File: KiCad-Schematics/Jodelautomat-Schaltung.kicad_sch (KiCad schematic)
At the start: 70 parts, among them J1 AudioJack3, J2 I2C_5V_01x04, J3 Barrel_Jack, J4 Screw_Terminal_01x02, J5 USART_Full_01x06, Q1 BC337, Q2 BC337, Q3 BC337, Q4 BC337, Q5 BC337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

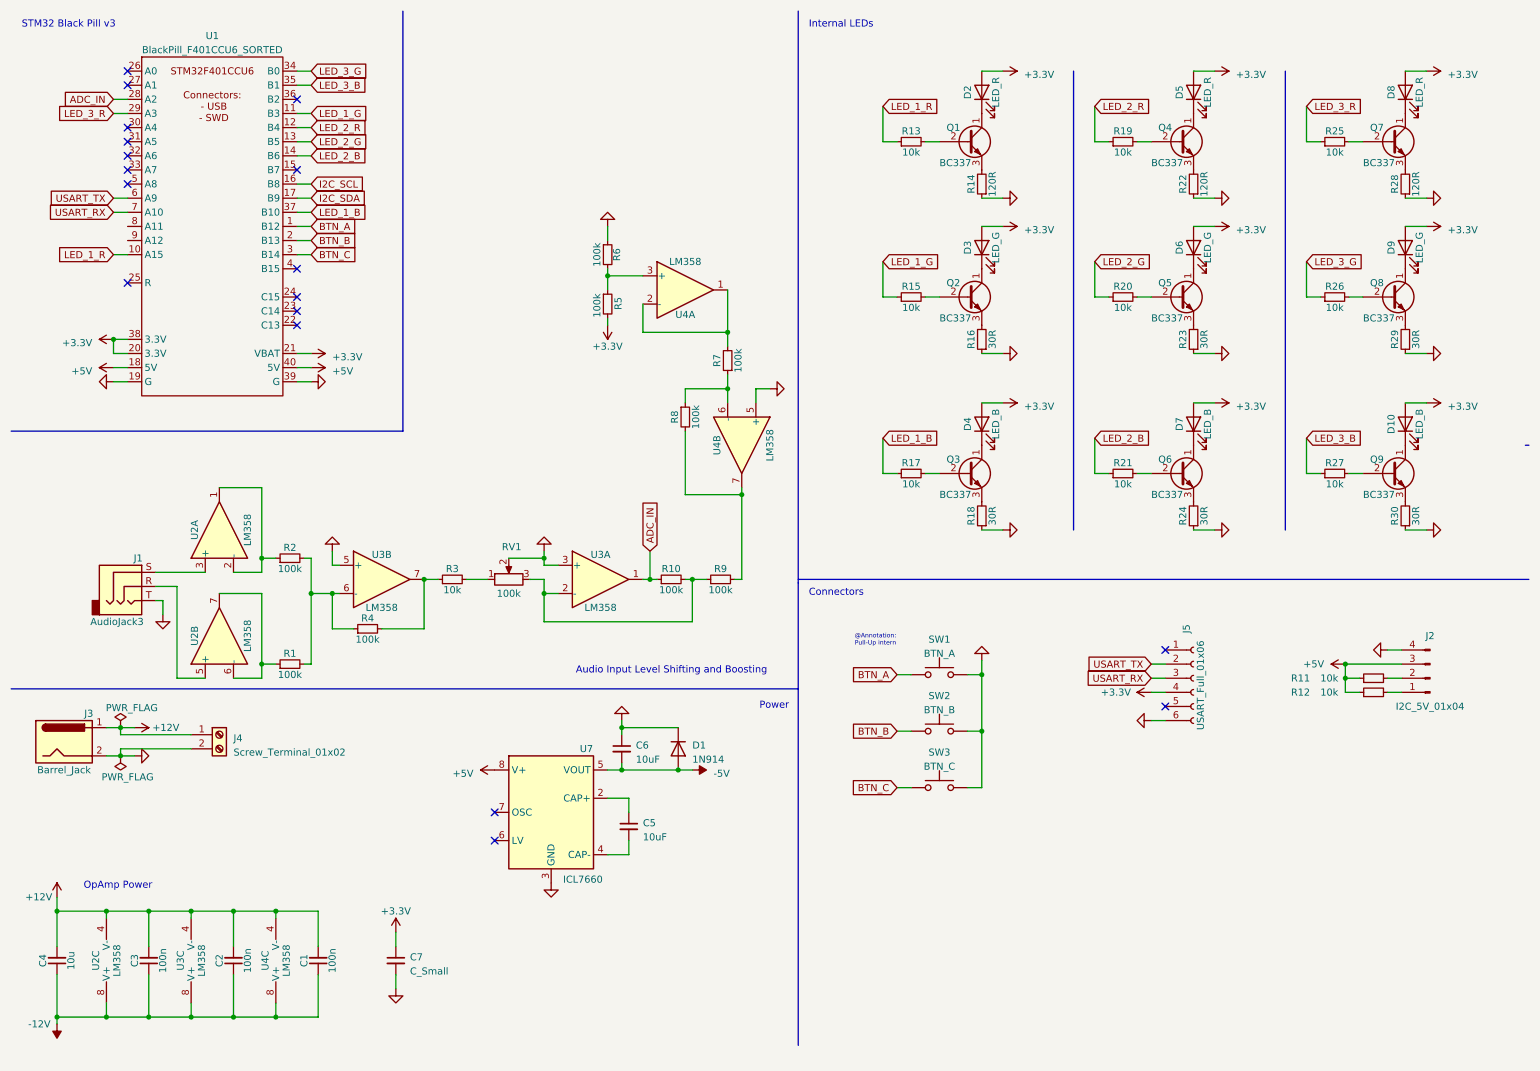
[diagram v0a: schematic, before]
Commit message: added uart fft output
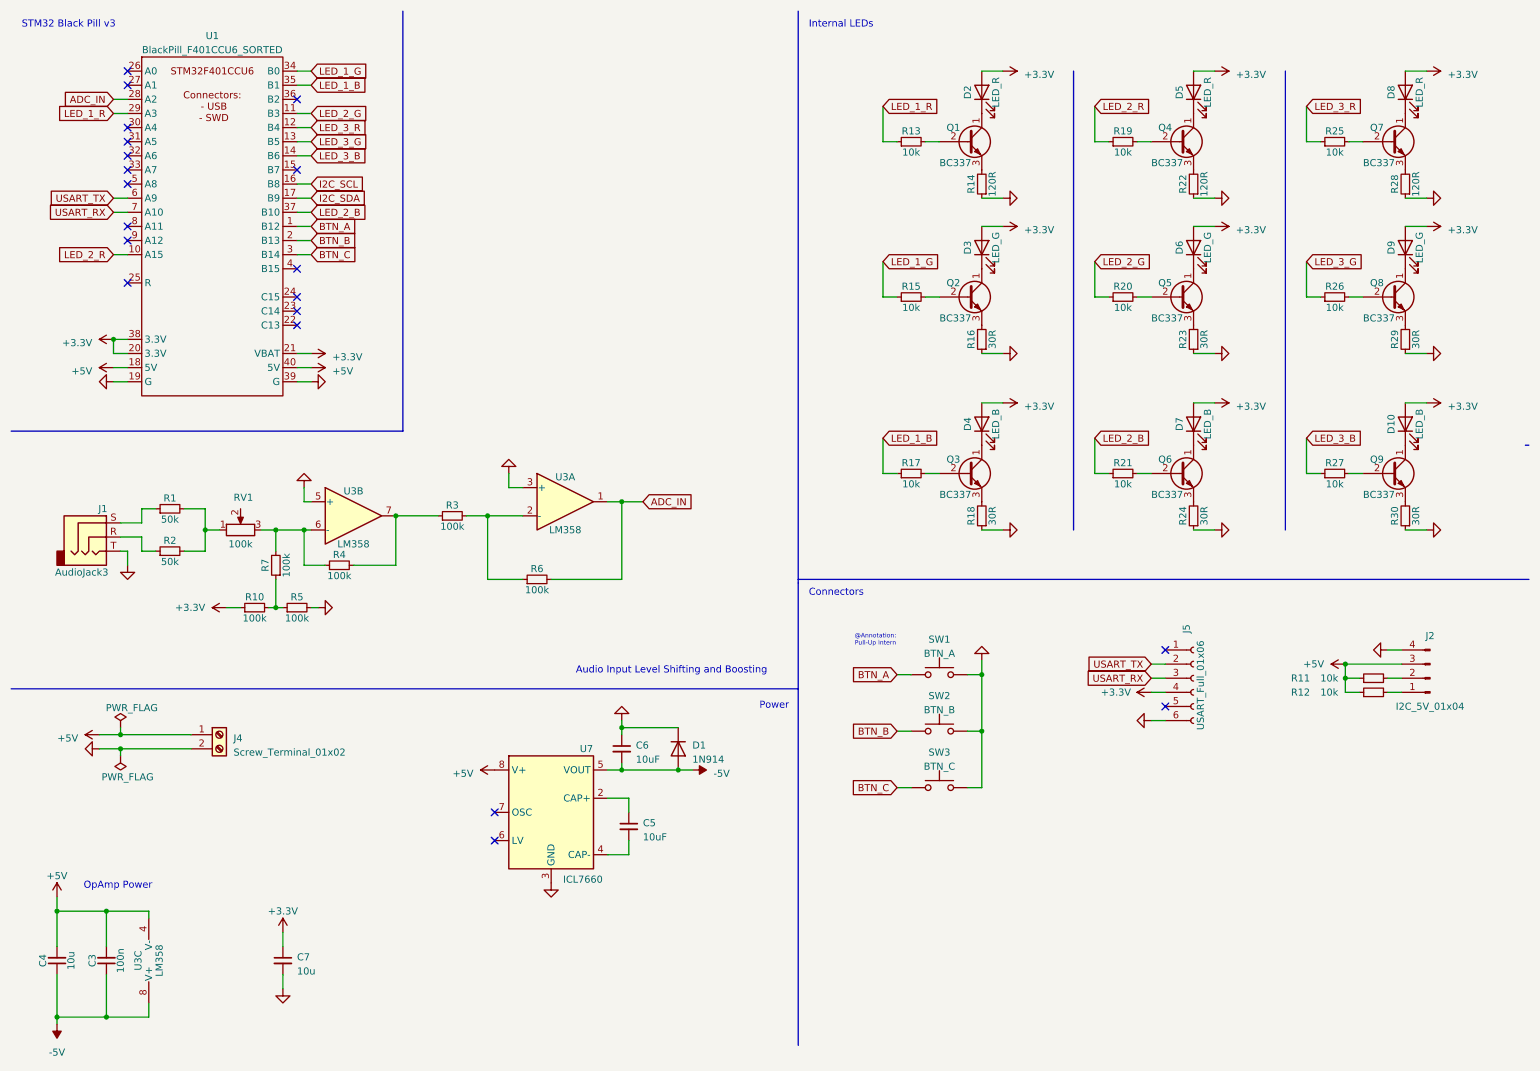
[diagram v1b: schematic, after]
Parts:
- removed C1, C2: 100n, Capacitor_SMD:C_0603_1608Metric, symbol Device:C_Small
- removed J3: Barrel_Jack, Connector_BarrelJack:BarrelJack_SwitchcraftConxall_RAPC10U_Horizontal, symbol Connector:Barrel_Jack
- removed R8, R9: 100k, Resistor_SMD:R_0402_1005Metric, symbol Device:R_Small
- removed U2, U4: LM358, Package_SO:SOIC-8_3.9x4.9mm_P1.27mm, symbol Amplifier_Operational:LM358
- C7: value C_Small -> 10u; footprint (none) -> Capacitor_SMD:C_0603_1608Metric
- D10, D2, D3, D4, D5, D6, D7, D8, D9: footprint (none) -> LED_SMD:LED_2010_5025Metric
- J2: footprint (none) -> Connector_Molex:Molex_PicoBlade_53047-0410_1x04_P1.25mm_Vertical
- J5: footprint (none) -> Connector_Molex:Molex_PicoBlade_53047-0610_1x06_P1.25mm_Vertical
- R1, R2: value 100k -> 50k
- R11, R12, R13, R15, R17, R19, R20, R21, R25, R26, R27: footprint (none) -> Resistor_SMD:R_0402_1005Metric
- R14, R16, R18, R22, R23, R24, R28, R29, R30: footprint (none) -> Resistor_SMD:R_0603_1608Metric
- R3: value 10k -> 100k
- SW1, SW2, SW3: footprint (none) -> Button_Switch_THT:SW_PUSH_6mm
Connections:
- net +12V is gone; now on net +5V: C3.2, C4.2, J4.1 (Pin_1), U3.4 (V-)
- net -12V is gone; now on net -5V: C3.1, C4.1, U3.8 (V+)
- net +3.3V: now also R10.1; no longer R5.2
- net ADC_IN: now also R6.2; no longer R10.1
- net GND: now also R5.2; no longer R6.1, RV1.2
- net LED_1_B: now also U1.35 (B1); no longer U1.37 (B10)
- net LED_1_G: now also U1.34 (B0); no longer U1.11 (B3)
- net LED_1_R: now also U1.29 (A3); no longer U1.10 (A15)
- net LED_2_B: now also U1.37 (B10); no longer U1.14 (B6)
- net LED_2_G: now also U1.11 (B3); no longer U1.13 (B5)
- net LED_2_R: now also U1.10 (A15); no longer U1.12 (B4)
- net LED_3_B: now also U1.14 (B6); no longer U1.35 (B1)
- net LED_3_G: now also U1.13 (B5); no longer U1.34 (B0)
- net LED_3_R: now also U1.12 (B4); no longer U1.29 (A3)
- net at R7.1: now also R10.2, R5.1
- net at R4.1, U3.6 (-): now also R7.2, RV1.3; no longer R1.2, R2.2
- net at RV1.1: now also R1.2, R2.2; no longer R3.2
- net at J1.R: now also R2.1
- net at R1.1: now also J1.S
- new net: R3.2, R6.1, U3.2 (-)
- no-connect marks 18 -> 20
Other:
- moved on the sheet: C3, C7, J1, R1, R10, R2, R4, RV1, U3A, U3B, U3C

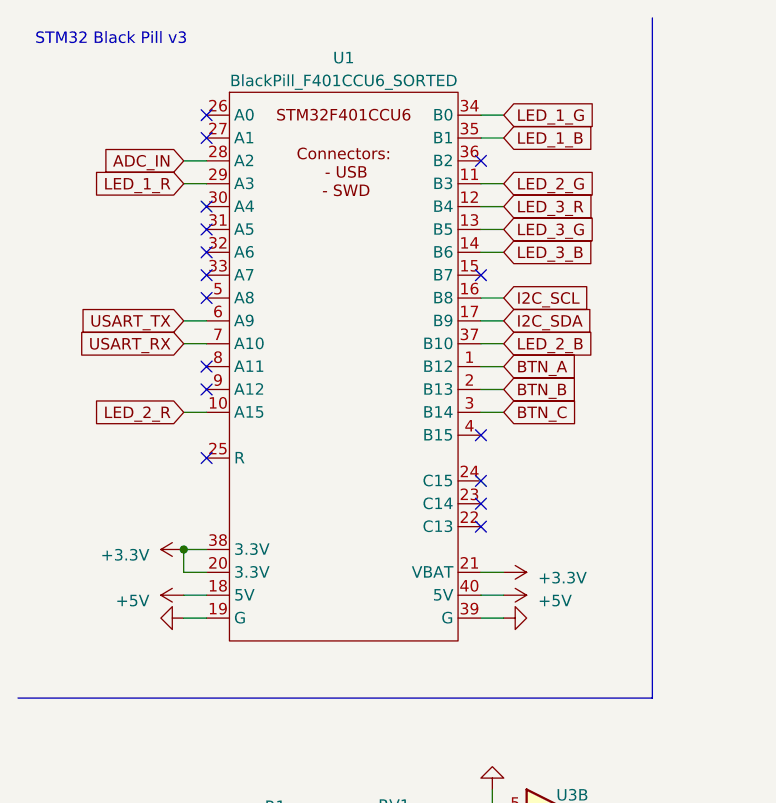
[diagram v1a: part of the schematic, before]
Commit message: moving pins around to have a better breadboard layout
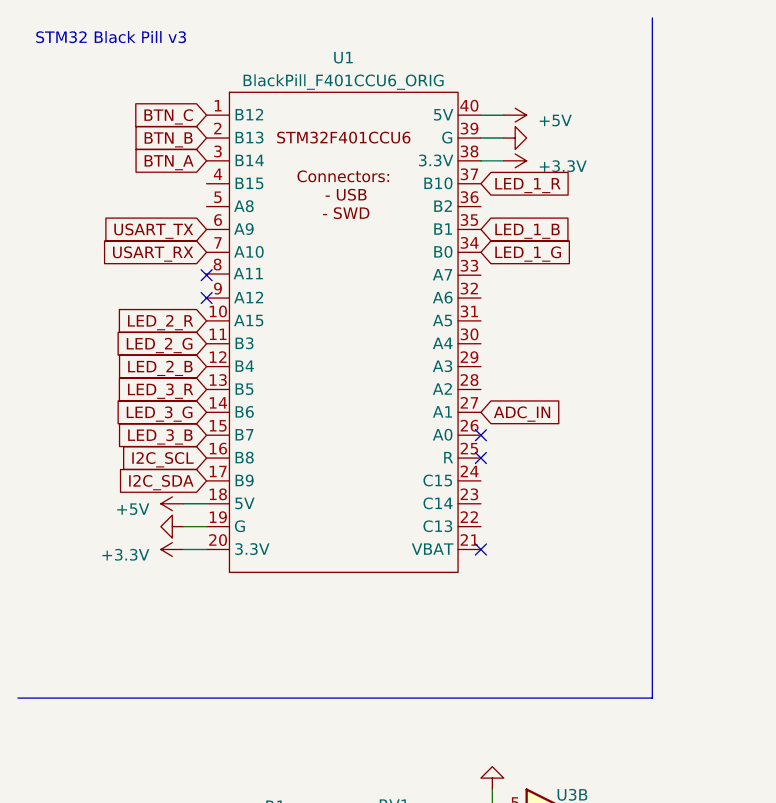
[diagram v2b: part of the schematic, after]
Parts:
- removed U1: BlackPill_F401CCU6_SORTED, STM32-Devboards:BlackPill_F401CCU6, symbol STM32-Devboards:BlackPill_F401CCU6_SORTED
- added U1: BlackPill_F401CCU6_ORIG, STM32-Devboards:BlackPill_F401CCU6, symbol STM32-Devboards:BlackPill_F401CCU6_ORIG
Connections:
- net +3.3V: now also U1.20 (3.3V), U1.38 (3.3V)
- net +5V: now also U1.18 (5V), U1.40 (5V)
- net ADC_IN: now also U1.27 (A1)
- net BTN_A: now also U1.3 (B14)
- net BTN_B: now also U1.2 (B13)
- net BTN_C: now also U1.1 (B12)
- net GND: now also U1.19 (G), U1.39 (G)
- net I2C_SCL: now also U1.16 (B8)
- net I2C_SDA: now also U1.17 (B9)
- net LED_1_B: now also U1.35 (B1)
- net LED_1_G: now also U1.34 (B0)
- net LED_1_R: now also U1.37 (B10)
- net LED_2_B: now also U1.12 (B4)
- net LED_2_G: now also U1.11 (B3)
- net LED_2_R: now also U1.10 (A15)
- net LED_3_B: now also U1.15 (B7)
- net LED_3_G: now also U1.14 (B6)
- net LED_3_R: now also U1.13 (B5)
- net USART_RX: now also U1.7 (A10)
- net USART_TX: now also U1.6 (A9)
- no-connect marks 20 -> 9
